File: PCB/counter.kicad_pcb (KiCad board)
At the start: 2 copper layers, 107.5 x 41 mm, 19 parts, among them P1 9V, Q1 2N3904, SW1 ПАУЗА, SW2 СБРОС, U1 4050, U2 LM7805, U3 ArduinoNano, U4 4_Digit_Display_Board, U5 Hall_Sensor

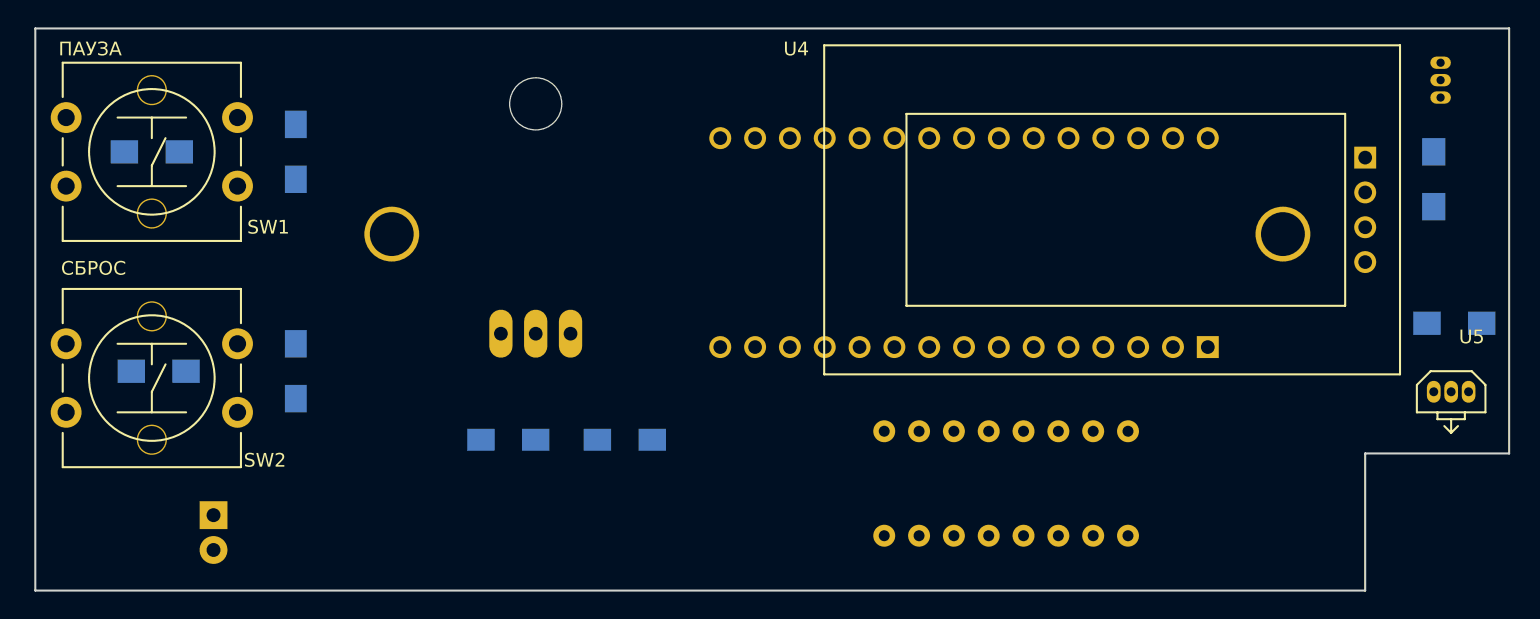
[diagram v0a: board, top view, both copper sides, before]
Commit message: Первое приближение разводки Добавил выключатель с фиксатором на батарейку
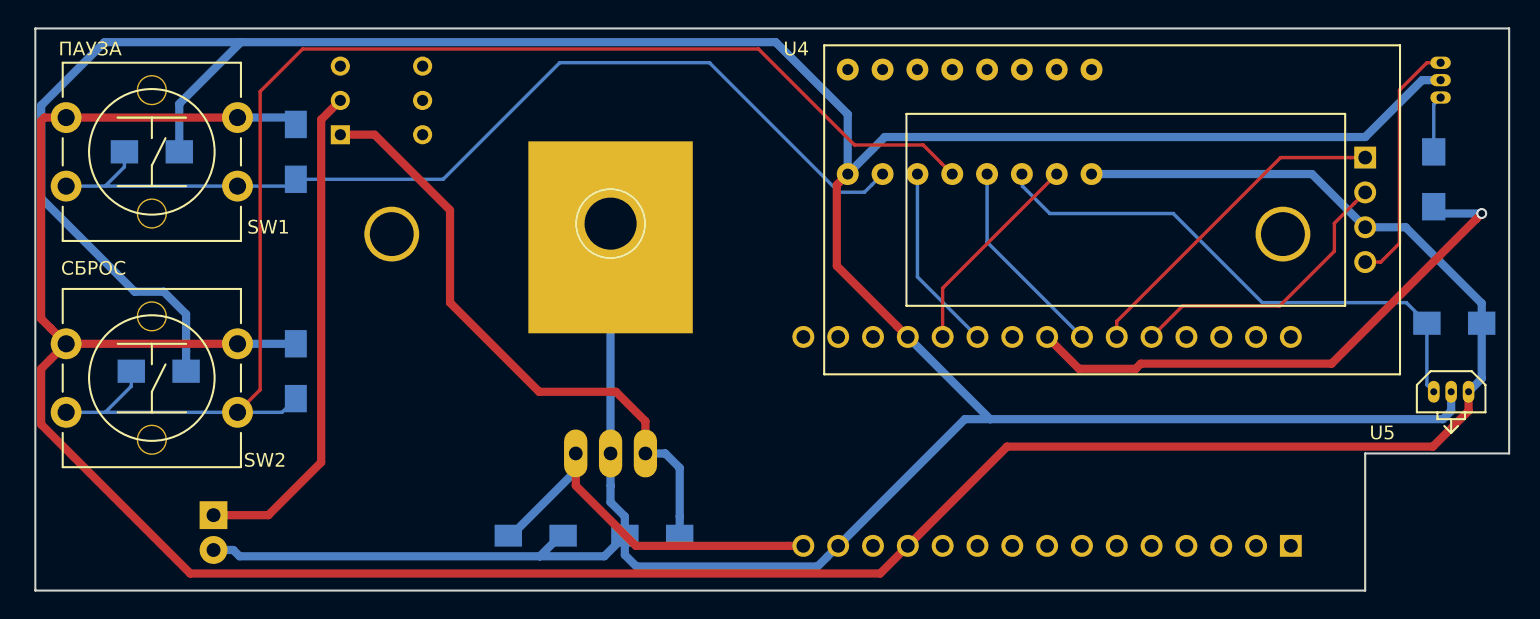
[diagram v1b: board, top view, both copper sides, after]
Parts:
- added SW3: Батарея, Buttons_Switches_ThroughHole:SW_PUSH_x2, B.Cu at (119.2, 53.2)
- U2: footprint TO_SOT_Packages_THT:TO-220_Neutral123_Horizontal_LargePads -> Libraries:LM7805_TO-220_Neutral123_Horizontal_LargePads_with_GND_pad
- moved U1 26.5 mm to (174.0, 56.1)
- moved U3 15.7 mm to (170.8, 75.6)
- moved U2 10.3 mm to (139.0, 76.5)
- moved C3 7.28 mm to (142.0, 82.5), turned to 0 degrees
- moved C4 7.28 mm to (133.5, 82.5)
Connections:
- P1 pad 1: +9V -> Net-(P1-Pad1)
- U1 pad 4: PAUSE_GOOD -> RESET_GOOD
- U1 pad 5: Net-(C1-Pad1) -> Net-(C2-Pad1)
- U1 pad 6: RESET_GOOD -> PAUSE_GOOD
- U1 pad 7: Net-(C2-Pad1) -> Net-(C1-Pad1)
- U3 pad 25: Net-(U3-Pad25) -> /DispCLK
- U3 pad 26: Net-(U3-Pad26) -> /DispDIO
- U4 pad 1: Net-(U3-Pad26) -> /DispCLK
- U4 pad 2: Net-(U3-Pad25) -> /DispDIO
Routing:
- net GND: track 0.00 -> 295.5 mm
- net +5V: track 0.00 -> 213.4 mm
- net Net-(C2-Pad1): track 0.00 -> 100.6 mm
- net Net-(C1-Pad1): track 0.00 -> 70.8 mm
- net +9V: track 0.00 -> 45.1 mm
- net /DispPower: track 0.00 -> 41.1 mm, vias 0 -> 1
- net SENSOR: track 0.00 -> 39.7 mm
- net Net-(P1-Pad1): track 0.00 -> 36.4 mm
- net +5VA: track 0.00 -> 28.9 mm
- net /DispCLK: track 0.00 -> 24.2 mm
- net /DispDIO: track 0.00 -> 21.6 mm
- net Net-(Q1-Pad3): track 0.00 -> 18.1 mm
- net SENSOR_GOOD: track 0.00 -> 15.3 mm
- net RESET_GOOD: track 0.00 -> 14.7 mm
- net PAUSE_GOOD: track 0.00 -> 13.7 mm
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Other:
- net class Default: via_dia 0.6 -> 0.7; via_drill 0.4 -> 0.45
- net class Power added: clearance 0.4, trace_width 0.6, via_dia 0.8, via_drill 0.5

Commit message: Добавил инкрементальную кнопку
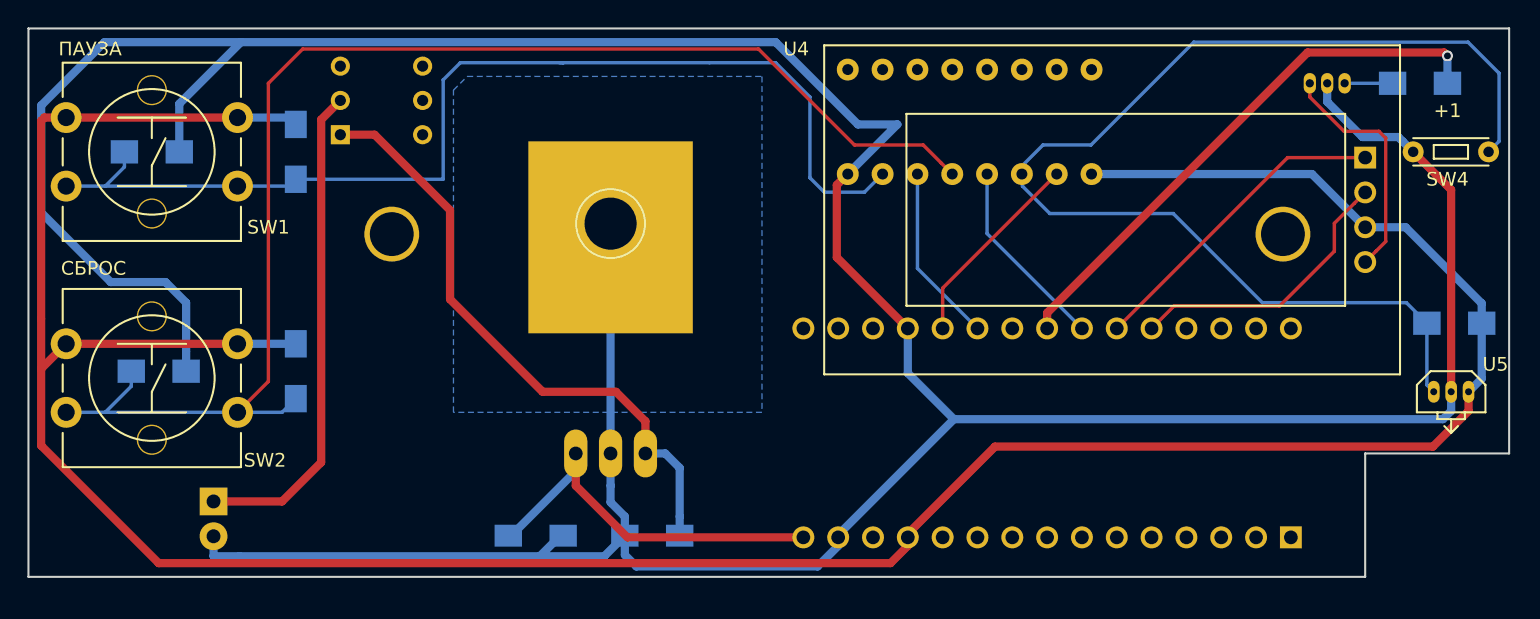
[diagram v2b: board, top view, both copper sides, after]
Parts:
- added SW4: +1, Libraries:Btn_Tack_5mm, F.Cu at (203.0, 54.5)
- moved Q1 7.08 mm to (192.5, 49.5), turned to 180 degrees
- moved R4 7.07 mm to (198.0, 49.5), turned to 180 degrees
- moved P1 1.00 mm to (110.0, 80.0)
- moved U3 0.62 mm to (170.8, 75.0)
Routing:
- net SENSOR: track 39.7 -> 85.9 mm
- net GND: track 295.5 -> 283.6 mm
- net Net-(C1-Pad1): track 70.8 -> 78.8 mm
- net +5V: track 213.4 -> 215.3 mm
- net /DispCLK: track 24.2 -> 23.3 mm
- net /DispPower: track 41.1 -> 40.3 mm
- net /DispDIO: track 21.6 -> 20.9 mm
- net Net-(Q1-Pad1): track 4.17 -> 3.50 mm
- net Net-(Q1-Pad3): track 18.1 -> 17.4 mm
- net SENSOR_GOOD: track 15.3 -> 14.7 mm
- net PAUSE_GOOD: track 13.7 -> 13.1 mm
- net RESET_GOOD: track 14.7 -> 14.1 mm
- added copper zone on B.Cu, net GND
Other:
- board size 107.5 x 41 mm -> 108 x 40 mm
